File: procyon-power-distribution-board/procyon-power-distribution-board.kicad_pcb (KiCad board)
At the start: 2 copper layers, 18 parts, among them Q1 BSS138, Q2 AO3401A, Q3 BSS138, Q4 AO3401A, Q5 BSS138, Q6 AO3401A, Q7 BSS138, Q8 AO3401A

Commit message: added more structure. wip commit
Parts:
- moved R9 49.2 mm to (161.3, 84.5), turned to -90 degrees
- moved Q8 48.9 mm to (159.2, 72.1)
- moved R8 48.2 mm to (159.2, 75.2)
- moved R7 46.7 mm to (156.3, 72.2), turned to 90 degrees
- moved Q6 44.5 mm to (148.2, 72.1)
- moved U1 43.8 mm to (142.2, 95.6)
- moved R6 43.6 mm to (148.2, 75.2)
- moved Q7 43.3 mm to (154.1, 69.6)
- moved R5 42.5 mm to (145.3, 72.2), turned to 90 degrees
- moved Q4 40.0 mm to (137.2, 72.1)
- moved Q5 39.3 mm to (143.1, 69.6)
- moved Q2 39.1 mm to (126.2, 72.1)
- moved R3 39.0 mm to (134.3, 72.2), turned to 90 degrees
- moved R4 38.9 mm to (137.2, 75.2)
- moved R2 38.5 mm to (123.3, 72.2), turned to 90 degrees
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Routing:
- net GND: track 0.00 -> 170.3 mm, vias 0 -> 21
- net +BATT: track 0.00 -> 62.0 mm
- net MCU_FPV_1: track 0.00 -> 47.9 mm, vias 0 -> 8
- net MCU_FPV_2: track 0.00 -> 36.0 mm, vias 0 -> 6
- net MCU_FPV_3: track 0.00 -> 24.4 mm, vias 0 -> 4
- net FPV_1_+: track 0.00 -> 13.3 mm
- net FPV_3_+: track 0.00 -> 13.3 mm
- net BLDC_1_+: track 0.00 -> 13.3 mm
- net FPV_2_+: track 0.00 -> 13.2 mm
- net MCU_BLDC_1: track 0.00 -> 13.0 mm, vias 0 -> 2
- net Net-(Q8-G): track 0.00 -> 4.23 mm
- net Net-(Q6-G): track 0.00 -> 4.23 mm
- net Net-(Q4-G): track 0.00 -> 4.23 mm
- net Net-(Q2-G): track 0.00 -> 4.23 mm
- net Net-(U1-EN): track 0.00 -> 3.83 mm
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
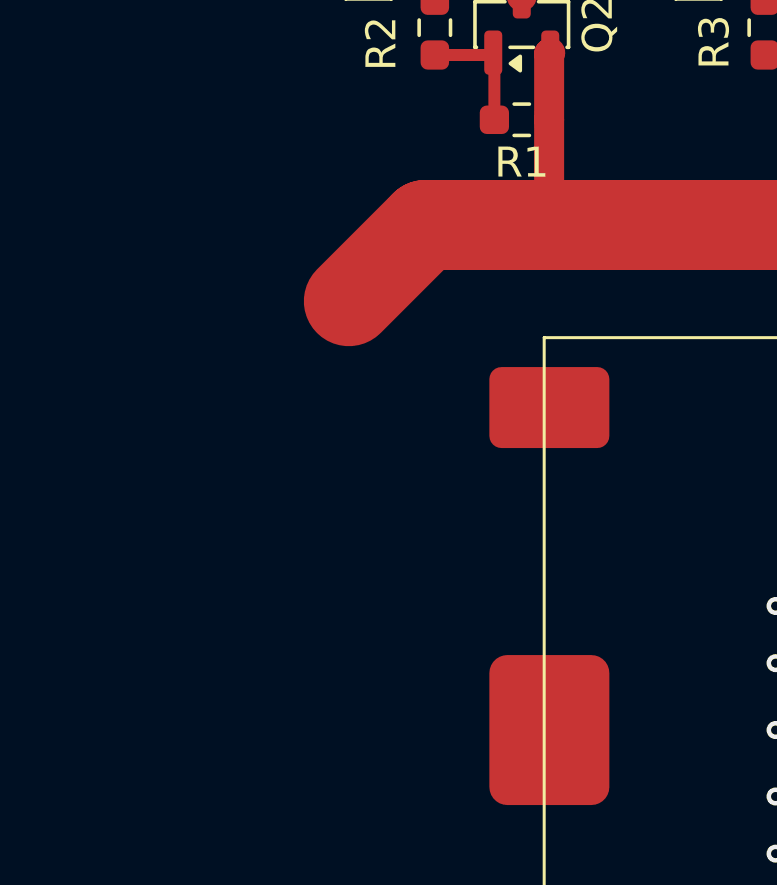
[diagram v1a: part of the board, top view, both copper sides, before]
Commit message: Mostly Done with Schematic. Need to wire up connectors (JST-XH???) and add some more filtering caps to the INA260
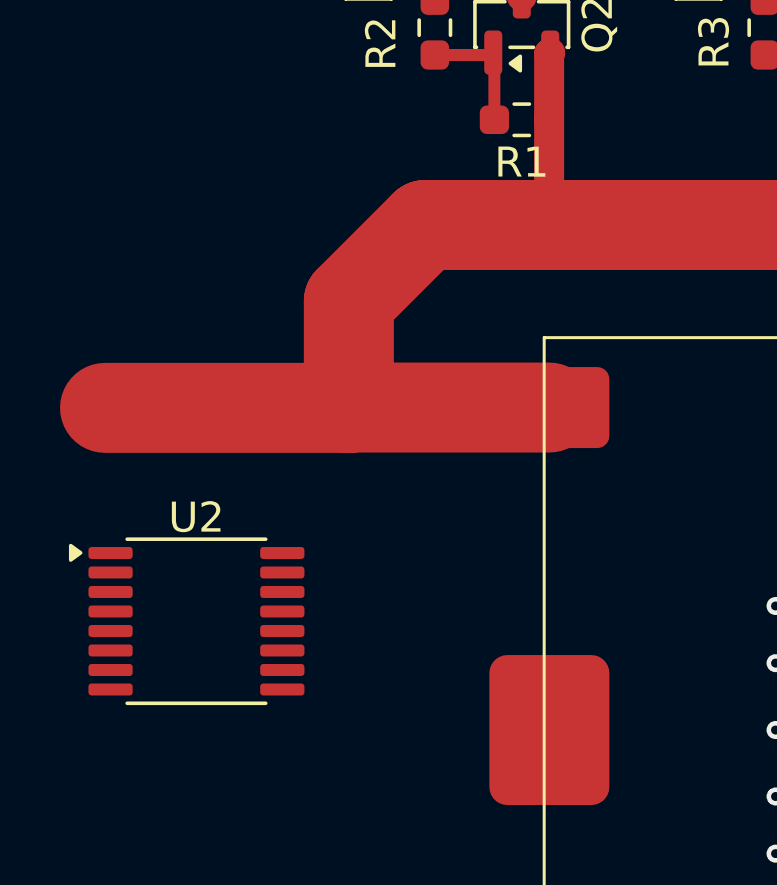
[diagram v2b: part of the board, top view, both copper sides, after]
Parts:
- added U2: INA260, Package_SO:TSSOP-16_4.4x5mm_P0.65mm, F.Cu at (115.3, 91.9)
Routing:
- net +BATT: track 62.0 -> 80.4 mm
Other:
- copper layers 2 -> 4

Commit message: Major changes, mostly finished, needs mounting holes and drc then finished.
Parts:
- added C1: 100nF, Capacitor_SMD:C_0603_1608Metric_Pad1.08x0.95mm_HandSolder, F.Cu at (121.3, 83.8)
- added J1: BLDC_Pwr, Connector_JST:JST_XH_S2B-XH-A-1_1x02_P2.50mm_Horizontal, F.Cu at (158.7, 62.9)
- added J10: XTRA2_PWR, Connector_JST:JST_XH_S2B-XH-A-1_1x02_P2.50mm_Horizontal, F.Cu at (169.5, 62.9)
- added J11: Ctrl_Header, Connector_JST:JST_XH_S6B-XH-A-1_1x06_P2.50mm_Horizontal, F.Cu at (170.8, 84.4)
- added J12: BATT_IN, Connector_Wire:SolderWire-1.5sqmm_1x02_P6mm_D1.7mm_OD3mm, F.Cu at (109.2, 78.7)
- added J2: FPV1_Pwr, Connector_JST:JST_XH_S2B-XH-A-1_1x02_P2.50mm_Horizontal, F.Cu at (126.3, 62.9)
- added J3: BDC_Pwr, Connector_JST:JST_XH_S2B-XH-A-1_1x02_P2.50mm_Horizontal, F.Cu at (115.6, 112.5)
- added J4: FPV2_Pwr, Connector_JST:JST_XH_S2B-XH-A-1_1x02_P2.50mm_Horizontal, F.Cu at (137.1, 62.9)
- added J5: FPV3_Pwr, Connector_JST:JST_XH_S2B-XH-A-1_1x02_P2.50mm_Horizontal, F.Cu at (147.9, 62.9)
- added J6: INA260_Header, Connector_JST:JST_XH_S6B-XH-A-1_1x06_P2.50mm_Horizontal, F.Cu at (170.8, 105.3)
- added J7: FC_PWR, Connector_JST:JST_XH_S2B-XH-A-1_1x02_P2.50mm_Horizontal, F.Cu at (127.6, 112.4)
- added J8: Radio_PWR, Connector_JST:JST_XH_S2B-XH-A-1_1x02_P2.50mm_Horizontal, F.Cu at (139.1, 112.4)
- added J9: XTRA1_PWR, Connector_JST:JST_XH_S2B-XH-A-1_1x02_P2.50mm_Horizontal, F.Cu at (151.1, 112.4)
- added Q10: AO3401A, Package_TO_SOT_SMD:SOT-23, F.Cu at (115.6, 103.5)
- added Q9: BSS138, Package_TO_SOT_SMD:SOT-23, F.Cu at (121.6, 105.7)
- added R12: 220, Resistor_SMD:R_0603_1608Metric_Pad0.98x0.95mm_HandSolder, F.Cu at (117.5, 106.4)
- added R13: 10k, Resistor_SMD:R_0603_1608Metric_Pad0.98x0.95mm_HandSolder, F.Cu at (118.4, 103.2)
- R2, R3, R5, R7: value 100 -> 220
- moved U2 11.0 mm to (116.5, 81.0)
- moved R9 1.91 mm to (163.2, 84.5), turned to 90 degrees
- moved U1 1.91 mm to (142.2, 93.7)
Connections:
- Q2 pad 3: FPV_1_+ -> Net-(J2-Pin_1)
- Q4 pad 3: FPV_2_+ -> Net-(J4-Pin_1)
- Q6 pad 3: FPV_3_+ -> Net-(J5-Pin_1)
- Q8 pad 3: BLDC_1_+ -> Net-(J1-Pin_1)
- U2 pad 10: +5V -> +3V3
- U2 pad 8: INA_SDA -> Net-(J6-Pin_2)
- U2 pad 9: INA_SCL -> Net-(J6-Pin_4)
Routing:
- net +5V: track 0.00 -> 92.4 mm
- net Net-(J6-Pin_2): track 0.00 -> 70.1 mm, vias 0 -> 1
- net MCU_DC_0: track 0.00 -> 69.8 mm, vias 0 -> 2
- net Net-(J6-Pin_4): track 0.00 -> 57.8 mm, vias 0 -> 1
- net +3V3: track 0.00 -> 56.1 mm, vias 0 -> 1
- net GND: track 170.3 -> 209.3 mm, vias 21 -> 43
- net +BATT: track 80.4 -> 115.4 mm
- net FPV_1_+: track 13.3 -> 0.00 mm
- net FPV_3_+: track 13.3 -> 0.00 mm
- net BLDC_1_+: track 13.3 -> 0.00 mm
- net FPV_2_+: track 13.2 -> 0.00 mm
- net Net-(J3-Pin_1): track 0.00 -> 9.33 mm
- net Net-(J1-Pin_1): track 0.00 -> 8.44 mm
- net Net-(J5-Pin_1): track 0.00 -> 8.36 mm
- net Net-(J2-Pin_1): track 0.00 -> 8.32 mm
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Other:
- board outline added: 80 x 66 mm

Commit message: V1 DONE!
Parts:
- added ?: , , F.Cu at (176.5, 57.1)
- added ?: , , F.Cu at (101.6, 118.1)
- added ?: , , F.Cu at (176.5, 118.1)
- added R10: 2.7k, Resistor_SMD:R_0603_1608Metric_Pad0.98x0.95mm_HandSolder, F.Cu at (118.1, 85.6)
- added R11: 2.7k, Resistor_SMD:R_0603_1608Metric_Pad0.98x0.95mm_HandSolder, F.Cu at (115.2, 85.6)
- added REF**: MountingHole_2.2mm_M2_Pad_Via, MountingHole:MountingHole_2.2mm_M2_Pad_Via, F.Cu at (176.5, 118.1)
- added REF**: MountingHole_2.2mm_M2_Pad_Via, MountingHole:MountingHole_2.2mm_M2_Pad_Via, F.Cu at (101.6, 118.1)
- added REF**: MountingHole_2.2mm_M2_Pad_Via, MountingHole:MountingHole_2.2mm_M2_Pad_Via, F.Cu at (176.5, 57.1)
- added REF**: MountingHole_2.2mm_M2_Pad_Via, MountingHole:MountingHole_2.2mm_M2_Pad_Via, F.Cu at (101.6, 57.1)
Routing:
- net +3V3: track 56.1 -> 68.4 mm
- net +BATT: track 115.4 -> 118.0 mm
- net Net-(J6-Pin_4): track 57.8 -> 60.4 mm
- net Net-(J6-Pin_2): track 70.1 -> 71.7 mm
- net GND: track 209.3 -> 208.0 mm, vias 43 -> 44
- added copper zone on In1.Cu, net GND
- added copper zone on In2.Cu, net GND
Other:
- outline, holes or cut-outs redrawn
- board text added: "+"
- board text added: "BATT+"
- board text added: "BATT-"
- board text added: "BLDC1"
- board text added: "DC1"
- board text added: "FC"
- board text added: "FPV1"
- board text added: "FPV2"
- board text added: "FPV3"
- board text added: "INA260"
- board text added: "PWR SWITCH"
- board text added: "RADIO"
- board text added: "XTRA_5V"
- board text added: "XTRA_7V4"
